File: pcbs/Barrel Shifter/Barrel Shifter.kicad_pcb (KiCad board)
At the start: 2 copper layers, 33 parts, among them U1001 74HC245, U1002 74HC245, U201 74HC138, U301 74HC245, U302 74HC245, U401 74HC245, U402 74HC245, U501 74HC245, U502 74HC245, U601 74HC245, U602 74HC245, U701 74HC245, U702 74HC245, U801 74HC245, U802 74HC245, U901 74HC245, U902 74HC245

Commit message: Second row
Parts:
- added D1201: Blue, LED_SMD:LED_0603_1608Metric, F.Cu at (73.3, 91.5)
- added D1301: Blue, LED_SMD:LED_0603_1608Metric, F.Cu at (101.2, 91.5)
- added D1401: Blue, LED_SMD:LED_0603_1608Metric, F.Cu at (126.0, 91.5)
- added D1501: Blue, LED_SMD:LED_0603_1608Metric, F.Cu at (149.5, 92.1)
- added D1601: Blue, LED_SMD:LED_0603_1608Metric, F.Cu at (175.5, 90.2)
- added D1701: Blue, LED_SMD:LED_0603_1608Metric, F.Cu at (201.5, 91.5)
- added D1801: Blue, LED_SMD:LED_0603_1608Metric, F.Cu at (225.7, 90.2)
- added D1901: Blue, LED_SMD:LED_0603_1608Metric, F.Cu at (252.3, 90.8)
- added R1201: 4k7, Resistor_SMD:R_0603_1608Metric, F.Cu at (77.3, 91.4)
- added R1301: 4k7, Resistor_SMD:R_0603_1608Metric, F.Cu at (105.2, 91.4)
- added R1401: 4k7, Resistor_SMD:R_0603_1608Metric, F.Cu at (130.0, 91.4)
- added R1501: 4k7, Resistor_SMD:R_0603_1608Metric, F.Cu at (153.5, 92.1)
- added R1601: 4k7, Resistor_SMD:R_0603_1608Metric, F.Cu at (179.5, 90.2)
- added R1701: 4k7, Resistor_SMD:R_0603_1608Metric, F.Cu at (205.6, 91.4)
- added R1801: 4k7, Resistor_SMD:R_0603_1608Metric, F.Cu at (229.7, 90.2)
- added R1901: 4k7, Resistor_SMD:R_0603_1608Metric, F.Cu at (256.4, 90.8)
- added U1201: 74HC245, Package_SO:SOIC-20W_7.5x12.8mm_P1.27mm, F.Cu at (76.2, 101.6)
- added U1202: 74HC245, Package_SO:SOIC-20W_7.5x12.8mm_P1.27mm, F.Cu at (76.2, 115.6)
- added U1301: 74HC245, Package_SO:SOIC-20W_7.5x12.8mm_P1.27mm, F.Cu at (101.6, 101.6)
- added U1302: 74HC245, Package_SO:SOIC-20W_7.5x12.8mm_P1.27mm, F.Cu at (101.6, 115.6)
- added U1401: 74HC245, Package_SO:SOIC-20W_7.5x12.8mm_P1.27mm, F.Cu at (127.0, 101.6)
- added U1402: 74HC245, Package_SO:SOIC-20W_7.5x12.8mm_P1.27mm, F.Cu at (127.0, 115.6)
- added U1501: 74HC245, Package_SO:SOIC-20W_7.5x12.8mm_P1.27mm, F.Cu at (152.4, 101.6)
- added U1502: 74HC245, Package_SO:SOIC-20W_7.5x12.8mm_P1.27mm, F.Cu at (152.4, 115.6)
- added U1601: 74HC245, Package_SO:SOIC-20W_7.5x12.8mm_P1.27mm, F.Cu at (177.8, 101.6)
- added U1602: 74HC245, Package_SO:SOIC-20W_7.5x12.8mm_P1.27mm, F.Cu at (177.8, 115.6)
- added U1701: 74HC245, Package_SO:SOIC-20W_7.5x12.8mm_P1.27mm, F.Cu at (203.2, 101.6)
- added U1702: 74HC245, Package_SO:SOIC-20W_7.5x12.8mm_P1.27mm, F.Cu at (203.2, 115.6)
- added U1801: 74HC245, Package_SO:SOIC-20W_7.5x12.8mm_P1.27mm, F.Cu at (228.6, 101.6)
- added U1802: 74HC245, Package_SO:SOIC-20W_7.5x12.8mm_P1.27mm, F.Cu at (228.6, 115.6)
- added U1901: 74HC245, Package_SO:SOIC-20W_7.5x12.8mm_P1.27mm, F.Cu at (254.0, 101.6)
- added U1902: 74HC245, Package_SO:SOIC-20W_7.5x12.8mm_P1.27mm, F.Cu at (254.0, 115.6)
- added U301: 74HC138, Package_DIP:DIP-16_W7.62mm_Socket, F.Cu at (43.2, 102.2)
- renumbered D901 to D1001, D1001 to D1101, D301 to D401, D401 to D501, D501 to D601, D601 to D701, D701 to D801, D801 to D901, R901 to R1001, R1001 to R1101, R301 to R401, R401 to R501, R501 to R601, R601 to R701, R701 to R801, R801 to R901, U901 to U1001, U902 to U1002, U1001 to U1101, U1002 to U1102, U301 to U401, U302 to U402, U401 to U501, U402 to U502, U501 to U601, U502 to U602, U601 to U701, U602 to U702, U701 to U801, U702 to U802, U801 to U901, U802 to U902
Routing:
- net /Shift Block 0/A0: track 507.6 -> 895.9 mm, vias 16 -> 24
- net /Shift Block 0/A1: track 487.9 -> 857.8 mm, vias 16 -> 24
- net /Shift Block 0/A2: track 470.8 -> 819.7 mm, vias 16 -> 24
- net /Shift Block 0/A3: track 467.0 -> 781.6 mm, vias 16 -> 24
- net /Shift Block 0/A4: track 442.9 -> 743.5 mm, vias 16 -> 24
- net /Shift Block 1/~{Y15}: track 0.00 -> 292.5 mm, vias 0 -> 4
- net /Shift Block 0/A5: track 430.2 -> 705.4 mm, vias 16 -> 24
- net /Shift Block 0/Out15: track 155.6 -> 415.4 mm, vias 0 -> 2
- net /Shift Block 0/Out14: track 155.6 -> 414.2 mm, vias 0 -> 2
- net /Shift Block 0/Out13: track 155.6 -> 412.8 mm, vias 0 -> 2
- net /Shift Block 0/Out12: track 155.6 -> 411.6 mm, vias 0 -> 2
- net /Shift Block 0/Out11: track 155.6 -> 410.3 mm, vias 0 -> 2
- net /Shift Block 0/Out10: track 155.6 -> 409.0 mm, vias 0 -> 2
- net /Shift Block 0/Out9: track 155.6 -> 407.7 mm, vias 0 -> 2
- net /Shift Block 0/Out8: track 155.6 -> 406.5 mm, vias 0 -> 2
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
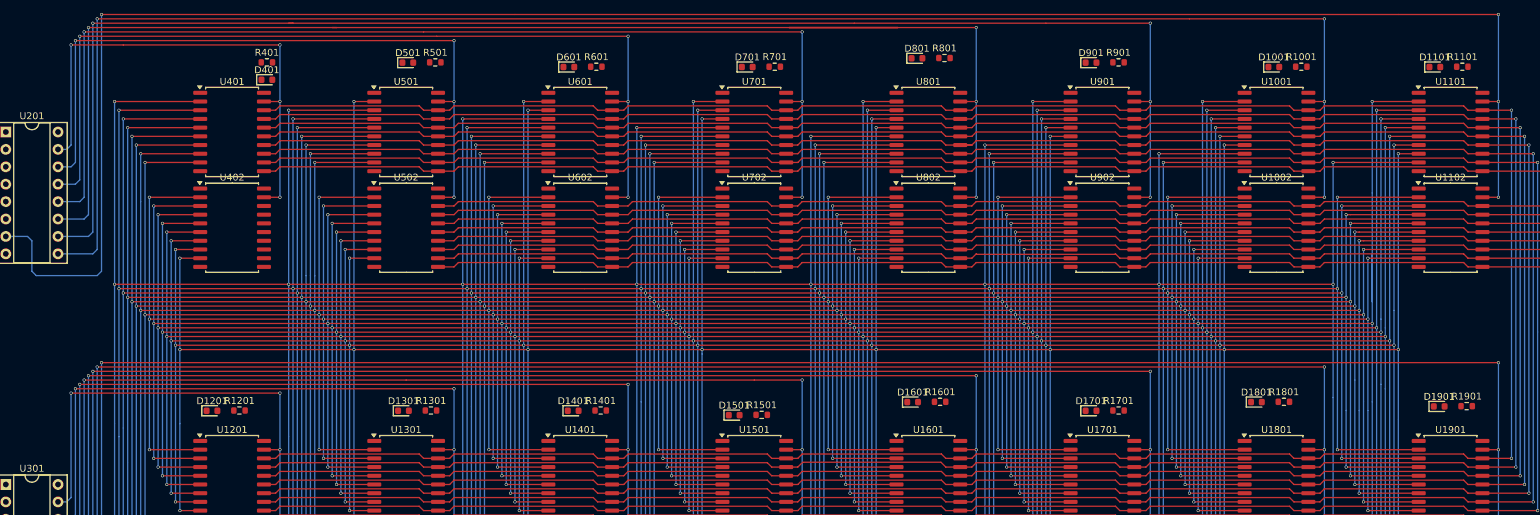
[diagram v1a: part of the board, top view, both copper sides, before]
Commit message: Starting to tidy up the LEDs
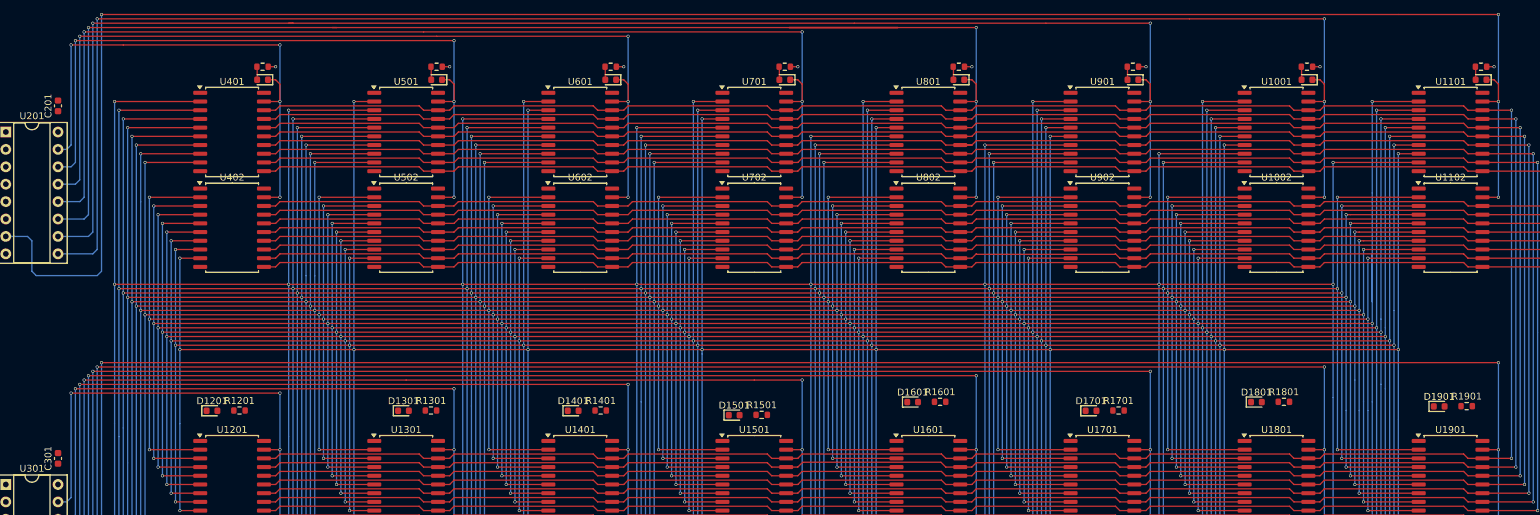
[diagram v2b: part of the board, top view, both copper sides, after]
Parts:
- added C201: C, Capacitor_SMD:C_0603_1608Metric, F.Cu at (50.8, 47.0)
- added C301: C, Capacitor_SMD:C_0603_1608Metric, F.Cu at (50.8, 98.4)
- moved D1101 6.99 mm to (258.4, 43.2), turned to 180 degrees
- moved D801 6.86 mm to (182.2, 43.2), turned to 180 degrees
- moved D901 6.60 mm to (207.6, 43.2), turned to 180 degrees
- moved D601 6.38 mm to (131.4, 43.2), turned to 180 degrees
- moved D701 5.78 mm to (156.8, 43.2), turned to 180 degrees
- moved D1001 5.18 mm to (233.0, 43.2), turned to 180 degrees
- moved D501 4.89 mm to (106.0, 43.2), turned to 180 degrees
- moved R1101 2.73 mm to (258.4, 41.3)
- moved R801 2.45 mm to (182.2, 41.3)
- moved R901 2.19 mm to (207.6, 41.3)
- moved R601 2.09 mm to (131.4, 41.3)
- moved R701 1.46 mm to (156.8, 41.3)
- moved R401 0.90 mm to (80.6, 41.3)
- moved R1001 0.82 mm to (233.0, 41.3)
- moved R501 0.66 mm to (106.0, 41.3)
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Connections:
- U201 pad 5: unconnected-(U201-~{E1}-Pad5) -> /Shift Block 0/~{Enable}
- U301 pad 5: unconnected-(U301-~{E1}-Pad5) -> /Shift Block 1/~{Enable}
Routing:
- net /Shift Block 0/Out8: track 406.5 -> 432.4 mm
- net /Shift Block 0/Out15: track 415.4 -> 441.4 mm
- net /Shift Block 0/Out14: track 414.2 -> 440.1 mm
- net /Shift Block 0/Out9: track 407.7 -> 433.7 mm
- net /Shift Block 0/Out13: track 412.8 -> 438.8 mm
- net /Shift Block 0/Out11: track 410.3 -> 436.2 mm
- net /Shift Block 0/Out10: track 409.0 -> 434.9 mm
- net /Shift Block 0/Out12: track 411.6 -> 437.5 mm
- net +5V: track 0.00 -> 8.64 mm, vias 0 -> 8
- net /Shift Block 0/~{Y5}: track 220.8 -> 225.4 mm
- net /Shift Block 0/~{Y7}: track 291.8 -> 296.4 mm
- net /Shift Block 0/~{Y4}: track 223.4 -> 227.9 mm
- net /Shift Block 0/~{Y2}: track 132.6 -> 137.1 mm
- net /Shift Block 0/~{Y1}: track 103.4 -> 107.9 mm
- net /Shift Block 0/~{Y0}: track 74.1 -> 78.7 mm
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
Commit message: Significant rethinking
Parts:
- removed C201, C301: C, Capacitor_SMD:C_0603_1608Metric
- removed D1001, D1101, D1201, D1301, D1401, D1501, D1601, D1701, D1801, D1901: Blue, LED_SMD:LED_0603_1608Metric
- removed R1001, R1101, R1201, R1301, R1401, R1501, R1601, R1701, R1801, R1901: 4k7, Resistor_SMD:R_0603_1608Metric
- removed U1001, U1002, U1101, U1102, U1201, U1202, U1301, U1302, U1401, U1402, U1501, U1502, U1601, U1602, U1701, U1702, U1801, U1802, U1901, U1902: 74HC245, Package_SO:SOIC-20W_7.5x12.8mm_P1.27mm
- added C101: C, Capacitor_SMD:C_0603_1608Metric, F.Cu at (48.1, 43.2)
- added D201: Blue, LED_SMD:LED_0603_1608Metric, F.Cu at (75.2, 41.3)
- added D301: Blue, LED_SMD:LED_0603_1608Metric, F.Cu at (100.6, 40.7)
- added R201: 4k7, Resistor_SMD:R_0603_1608Metric, F.Cu at (79.2, 41.3)
- added R301: 4k7, Resistor_SMD:R_0603_1608Metric, F.Cu at (104.6, 40.6)
- added U101: 74HC138, Package_DIP:DIP-16_W7.62mm_Socket, F.Cu at (45.7, 50.8)
- added U202: 74HC245, Package_SO:SOIC-20W_7.5x12.8mm_P1.27mm, F.Cu at (76.0, 64.8)
- added U302: 74HC245, Package_SO:SOIC-20W_7.5x12.8mm_P1.27mm, F.Cu at (101.6, 64.8)
- U201, U301: value 74HC138 -> 74HC245; footprint Package_DIP:DIP-16_W7.62mm_Socket -> Package_SO:SOIC-20W_7.5x12.8mm_P1.27mm
- moved U301 77.8 mm to (101.6, 50.8)
- moved D901 75.5 mm to (150.1, 92.1), turned to 0 degrees
- moved D601 74.2 mm to (74.5, 90.8), turned to 0 degrees
- moved D701 74.2 mm to (100.6, 91.5), turned to 0 degrees
- moved R901 73.8 mm to (154.1, 92.1)
- moved D801 73.2 mm to (127.2, 91.5), turned to 0 degrees
- moved R601 72.5 mm to (78.5, 90.8)
- moved R701 72.4 mm to (104.6, 91.4)
- moved U701 71.8 mm to (101.6, 101.6)
- moved U702 71.8 mm to (101.6, 115.6)
- moved U801 71.8 mm to (127.0, 101.6)
- moved U802 71.8 mm to (127.0, 115.6)
- moved U601 71.8 mm to (76.2, 101.6)
- moved U602 71.8 mm to (76.2, 115.6)
- moved U901 71.8 mm to (152.4, 101.6)
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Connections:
- net /Shift Block 0/A0 renamed /A14
- net /Shift Block 0/A10 renamed /A8
- net /Shift Block 0/A11 renamed /A9
- net /Shift Block 0/A12 renamed /A10
- net /Shift Block 0/A13 renamed /A11
- net /Shift Block 0/A14 renamed /A12
- net /Shift Block 0/A15 renamed /A13
- net /Shift Block 0/Out10 renamed /Out10
- net /Shift Block 0/Out11 renamed /Out11
- net /Shift Block 0/Out12 renamed /Out12
- net /Shift Block 0/Out13 renamed /Out13
- net /Shift Block 0/Out14 renamed /Out14
- net /Shift Block 0/Out15 renamed /Out15
- net /Shift Block 0/Out8 renamed /Out8
- net /Shift Block 0/Out9 renamed /Out9
- D401 pad 1: /Shift Block 0/~{Y0} -> /~{Y2}
- D501 pad 1: /Shift Block 0/~{Y1} -> /~{Y3}
- D601 pad 1: /Shift Block 0/~{Y2} -> /~{Y4}
- D701 pad 1: /Shift Block 0/~{Y3} -> /~{Y5}
- D801 pad 1: /Shift Block 0/~{Y4} -> /~{Y6}
- D901 pad 1: /Shift Block 0/~{Y5} -> /~{Y7}
- U201 pad 1: unconnected-(U201-A0-Pad1) -> +5V
- U201 pad 10: /Shift Block 0/~{Y5} -> GND
- U201 pad 11: /Shift Block 0/~{Y4} -> /Out7
- U201 pad 12: /Shift Block 0/~{Y3} -> /Out6
- U201 pad 13: /Shift Block 0/~{Y2} -> /Out5
- U201 pad 14: /Shift Block 0/~{Y1} -> /Out4
- U201 pad 15: /Shift Block 0/~{Y0} -> /Out3
- U201 pad 16: +5V -> /Out2
- U201 pad 2: unconnected-(U201-A1-Pad2) -> /A0
- U201 pad 3: unconnected-(U201-A2-Pad3) -> /A1
- U201 pad 4: unconnected-(U201-~{E0}-Pad4) -> /A2
- U201 pad 5: /Shift Block 0/~{Enable} -> /A3
- U201 pad 6: unconnected-(U201-E2-Pad6) -> /A4
- U201 pad 7: /Shift Block 0/~{Y7} -> /A5
- U201 pad 8: GND -> /A6
- U201 pad 9: /Shift Block 0/~{Y6} -> /A7
- U301 pad 1: unconnected-(U301-A0-Pad1) -> +5V
- U301 pad 10: /Shift Block 1/~{Y13} -> GND
- U301 pad 11: /Shift Block 1/~{Y12} -> /Out7
- U301 pad 12: /Shift Block 1/~{Y11} -> /Out6
- U301 pad 13: /Shift Block 1/~{Y10} -> /Out5
- U301 pad 14: /Shift Block 1/~{Y9} -> /Out4
- U301 pad 15: /Shift Block 1/~{Y8} -> /Out3
- U301 pad 16: +5V -> /Out2
- U301 pad 2: unconnected-(U301-A1-Pad2) -> /A15
- U301 pad 3: unconnected-(U301-A2-Pad3) -> /A0
- U301 pad 4: unconnected-(U301-~{E0}-Pad4) -> /A1
- U301 pad 5: /Shift Block 1/~{Enable} -> /A2
- U301 pad 6: unconnected-(U301-E2-Pad6) -> /A3
- U301 pad 7: /Shift Block 1/~{Y15} -> /A4
- U301 pad 8: GND -> /A5
- U301 pad 9: /Shift Block 1/~{Y14} -> /A6
- U401 pad 11: /Shift Block 0/Out7 -> /Out7
- U401 pad 12: /Shift Block 0/Out6 -> /Out6
- U401 pad 13: /Shift Block 0/Out5 -> /Out5
- U401 pad 14: /Shift Block 0/Out4 -> /Out4
- U401 pad 15: /Shift Block 0/Out3 -> /Out3
- U401 pad 16: /Shift Block 0/Out2 -> /Out2
- U401 pad 17: /Shift Block 0/Out1 -> /Out1
- U401 pad 18: /Shift Block 0/Out0 -> /Out0
- U401 pad 19: /Shift Block 0/~{Y0} -> /~{Y2}
- U401 pad 3: /Shift Block 0/A1 -> /A15
- U401 pad 4: /Shift Block 0/A2 -> /A0
- U401 pad 5: /Shift Block 0/A3 -> /A1
- U401 pad 6: /Shift Block 0/A4 -> /A2
- U401 pad 7: /Shift Block 0/A5 -> /A3
- U401 pad 8: /Shift Block 0/A6 -> /A4
- U401 pad 9: /Shift Block 0/A7 -> /A5
- U402 pad 19: /Shift Block 0/~{Y0} -> /~{Y2}
- U402 pad 2: /Shift Block 0/A8 -> /A6
- U402 pad 3: /Shift Block 0/A9 -> /A7
- U501 pad 11: /Shift Block 0/Out7 -> /Out7
- U501 pad 12: /Shift Block 0/Out6 -> /Out6
- U501 pad 13: /Shift Block 0/Out5 -> /Out5
- U501 pad 14: /Shift Block 0/Out4 -> /Out4
- U501 pad 15: /Shift Block 0/Out3 -> /Out3
- U501 pad 16: /Shift Block 0/Out2 -> /Out2
- U501 pad 17: /Shift Block 0/Out1 -> /Out1
- U501 pad 18: /Shift Block 0/Out0 -> /Out0
- U501 pad 19: /Shift Block 0/~{Y1} -> /~{Y3}
- U501 pad 4: /Shift Block 0/A1 -> /A15
- U501 pad 5: /Shift Block 0/A2 -> /A0
- U501 pad 6: /Shift Block 0/A3 -> /A1
- U501 pad 7: /Shift Block 0/A4 -> /A2
- U501 pad 8: /Shift Block 0/A5 -> /A3
- U501 pad 9: /Shift Block 0/A6 -> /A4
- U502 pad 19: /Shift Block 0/~{Y1} -> /~{Y3}
- U502 pad 2: /Shift Block 0/A7 -> /A5
- U502 pad 3: /Shift Block 0/A8 -> /A6
- U502 pad 4: /Shift Block 0/A9 -> /A7
- U601 pad 11: /Shift Block 0/Out7 -> /Out7
- U601 pad 12: /Shift Block 0/Out6 -> /Out6
- U601 pad 13: /Shift Block 0/Out5 -> /Out5
- U601 pad 14: /Shift Block 0/Out4 -> /Out4
- U601 pad 15: /Shift Block 0/Out3 -> /Out3
- U601 pad 16: /Shift Block 0/Out2 -> /Out2
- U601 pad 17: /Shift Block 0/Out1 -> /Out1
- U601 pad 18: /Shift Block 0/Out0 -> /Out0
- U601 pad 19: /Shift Block 0/~{Y2} -> /~{Y4}
- U601 pad 5: /Shift Block 0/A1 -> /A15
- U601 pad 6: /Shift Block 0/A2 -> /A0
- U601 pad 7: /Shift Block 0/A3 -> /A1
- U601 pad 8: /Shift Block 0/A4 -> /A2
- U601 pad 9: /Shift Block 0/A5 -> /A3
- U602 pad 19: /Shift Block 0/~{Y2} -> /~{Y4}
- U602 pad 2: /Shift Block 0/A6 -> /A4
- U602 pad 3: /Shift Block 0/A7 -> /A5
- U602 pad 4: /Shift Block 0/A8 -> /A6
- U602 pad 5: /Shift Block 0/A9 -> /A7
- U701 pad 11: /Shift Block 0/Out7 -> /Out7
- U701 pad 12: /Shift Block 0/Out6 -> /Out6
- U701 pad 13: /Shift Block 0/Out5 -> /Out5
- U701 pad 14: /Shift Block 0/Out4 -> /Out4
- U701 pad 15: /Shift Block 0/Out3 -> /Out3
- U701 pad 16: /Shift Block 0/Out2 -> /Out2
- U701 pad 17: /Shift Block 0/Out1 -> /Out1
- U701 pad 18: /Shift Block 0/Out0 -> /Out0
- U701 pad 19: /Shift Block 0/~{Y3} -> /~{Y5}
- U701 pad 6: /Shift Block 0/A1 -> /A15
- U701 pad 7: /Shift Block 0/A2 -> /A0
- U701 pad 8: /Shift Block 0/A3 -> /A1
- U701 pad 9: /Shift Block 0/A4 -> /A2
- U702 pad 19: /Shift Block 0/~{Y3} -> /~{Y5}
- U702 pad 2: /Shift Block 0/A5 -> /A3
- U702 pad 3: /Shift Block 0/A6 -> /A4
- U702 pad 4: /Shift Block 0/A7 -> /A5
- U702 pad 5: /Shift Block 0/A8 -> /A6
- U702 pad 6: /Shift Block 0/A9 -> /A7
- U801 pad 11: /Shift Block 0/Out7 -> /Out7
- U801 pad 12: /Shift Block 0/Out6 -> /Out6
- U801 pad 13: /Shift Block 0/Out5 -> /Out5
- U801 pad 14: /Shift Block 0/Out4 -> /Out4
- U801 pad 15: /Shift Block 0/Out3 -> /Out3
- U801 pad 16: /Shift Block 0/Out2 -> /Out2
- U801 pad 17: /Shift Block 0/Out1 -> /Out1
- U801 pad 18: /Shift Block 0/Out0 -> /Out0
- U801 pad 19: /Shift Block 0/~{Y4} -> /~{Y6}
- U801 pad 7: /Shift Block 0/A1 -> /A15
- U801 pad 8: /Shift Block 0/A2 -> /A0
- U801 pad 9: /Shift Block 0/A3 -> /A1
- U802 pad 19: /Shift Block 0/~{Y4} -> /~{Y6}
- U802 pad 2: /Shift Block 0/A4 -> /A2
- U802 pad 3: /Shift Block 0/A5 -> /A3
- U802 pad 4: /Shift Block 0/A6 -> /A4
- U802 pad 5: /Shift Block 0/A7 -> /A5
- U802 pad 6: /Shift Block 0/A8 -> /A6
- U802 pad 7: /Shift Block 0/A9 -> /A7
- U901 pad 11: /Shift Block 0/Out7 -> /Out7
- U901 pad 12: /Shift Block 0/Out6 -> /Out6
- U901 pad 13: /Shift Block 0/Out5 -> /Out5
- U901 pad 14: /Shift Block 0/Out4 -> /Out4
- U901 pad 15: /Shift Block 0/Out3 -> /Out3
- U901 pad 16: /Shift Block 0/Out2 -> /Out2
- U901 pad 17: /Shift Block 0/Out1 -> /Out1
- U901 pad 18: /Shift Block 0/Out0 -> /Out0
- U901 pad 19: /Shift Block 0/~{Y5} -> /~{Y7}
- U901 pad 8: /Shift Block 0/A1 -> /A15
- U901 pad 9: /Shift Block 0/A2 -> /A0
- U902 pad 19: /Shift Block 0/~{Y5} -> /~{Y7}
- U902 pad 2: /Shift Block 0/A3 -> /A1
- U902 pad 3: /Shift Block 0/A4 -> /A2
- U902 pad 4: /Shift Block 0/A5 -> /A3
- U902 pad 5: /Shift Block 0/A6 -> /A4
- U902 pad 6: /Shift Block 0/A7 -> /A5
- U902 pad 7: /Shift Block 0/A8 -> /A6
- U902 pad 8: /Shift Block 0/A9 -> /A7
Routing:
- net /Shift Block 0/A1: track 857.8 -> 0.00 mm, vias 24 -> 0
- net /Shift Block 0/A2: track 819.7 -> 0.00 mm, vias 24 -> 0
- net /Shift Block 0/A3: track 781.6 -> 0.00 mm, vias 24 -> 0
- net /Shift Block 0/A4: track 743.5 -> 0.00 mm, vias 24 -> 0
- net /Shift Block 0/A5: track 705.4 -> 0.00 mm, vias 24 -> 0
- net /Shift Block 0/A6: track 667.3 -> 0.00 mm, vias 24 -> 0
- net /Shift Block 0/A7: track 629.2 -> 0.00 mm, vias 24 -> 0
- net /Shift Block 0/A9: track 622.8 -> 0.00 mm, vias 24 -> 0
- net /A14: track 895.9 -> 273.1 mm, vias 24 -> 12
- net /Shift Block 0/A8: track 591.1 -> 0.00 mm, vias 24 -> 0
- net /A12: track 697.8 -> 232.4 mm, vias 24 -> 12
- net /A13: track 715.5 -> 252.8 mm, vias 24 -> 12
- net /Shift Block 0/Out7: track 431.1 -> 0.00 mm, vias 2 -> 0
- net /Shift Block 0/Out6: track 429.9 -> 0.00 mm, vias 2 -> 0
- net /Shift Block 0/Out4: track 429.4 -> 0.00 mm, vias 2 -> 0
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
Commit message: Almost there...
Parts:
- added J101: ~, BoardEdgeConnectors:TE-5530843-4-Edge, F.Cu at (25.4, 78.7)
- moved D401 6.99 mm to (131.4, 42.5), turned to 180 degrees
- moved D501 6.86 mm to (156.8, 42.5), turned to 180 degrees
- moved D901 6.85 mm to (156.8, 93.3), turned to 180 degrees
- moved D601 6.60 mm to (80.6, 93.3), turned to 180 degrees
- moved C101 6.11 mm to (53.3, 46.4), turned to 90 degrees
- moved D301 5.78 mm to (106.0, 42.5), turned to 180 degrees
- moved D701 5.78 mm to (106.0, 93.3), turned to 180 degrees
- moved D201 5.61 mm to (80.6, 42.5), turned to 180 degrees
- moved D801 4.60 mm to (131.4, 93.3), turned to 180 degrees
- moved R901 2.80 mm to (156.8, 91.4)
- moved R401 2.73 mm to (131.4, 40.6)
- moved R501 2.45 mm to (156.8, 40.6)
- moved R601 2.19 mm to (80.6, 91.4)
- moved R201 1.59 mm to (80.6, 40.6)
- moved R301 1.46 mm to (106.0, 40.6)
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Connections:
- net /Out0 renamed /C0
- net /Out1 renamed /C1
- net /Out10 renamed /C10
- net /Out11 renamed /C11
- net /Out12 renamed /C12
- net /Out13 renamed /C13
- net /Out14 renamed /C14
- net /Out15 renamed /C15
- net /Out2 renamed /C2
- net /Out3 renamed /C3
- net /Out4 renamed /C4
- net /Out5 renamed /C5
- net /Out6 renamed /C6
- net /Out7 renamed /C7
- net /Out8 renamed /C8
- net /Out9 renamed /C9
- U101 pad 1: unconnected-(U101-A0-Pad1) -> /B_0
- U101 pad 2: unconnected-(U101-A1-Pad2) -> /B_1
- U101 pad 3: unconnected-(U101-A2-Pad3) -> /B_2
- U101 pad 4: unconnected-(U101-~{E0}-Pad4) -> /B_3
- U101 pad 5: /~{Enable} -> /~{OE}
- U101 pad 6: unconnected-(U101-E2-Pad6) -> +5V
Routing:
- net /C12: track 77.8 -> 379.0 mm, vias 0 -> 3
- net /C8: track 77.8 -> 373.3 mm, vias 0 -> 3
- net /C10: track 77.8 -> 372.0 mm, vias 0 -> 3
- net /C14: track 77.8 -> 370.1 mm, vias 0 -> 3
- net /C3: track 77.8 -> 366.6 mm, vias 0 -> 3
- net /C2: track 77.8 -> 360.6 mm, vias 0 -> 3
- net /C4: track 77.8 -> 359.9 mm, vias 0 -> 3
- net /C6: track 77.8 -> 358.6 mm, vias 0 -> 3
- net /C9: track 77.8 -> 356.5 mm, vias 0 -> 3
- net /C13: track 77.8 -> 356.5 mm, vias 0 -> 3
- net /C11: track 77.8 -> 355.8 mm, vias 0 -> 3
- net /C0: track 103.7 -> 369.4 mm, vias 0 -> 3
- net /C5: track 77.8 -> 340.6 mm, vias 0 -> 3
- net /C1: track 77.8 -> 340.0 mm, vias 0 -> 3
- net +5V: track 0.00 -> 225.9 mm, vias 0 -> 25
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- added copper zone on B.Cu, net +5V
- added copper zone on F.Cu, net GND
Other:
- board outline added: 132.1 x 100.3 mm
- board text added: "Barrel Shifter"
- board text added: "JLCJLCJLCJLC"
- board text added: "RGE2024"

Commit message: Finishing connection
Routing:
- net GND: track 6.25 -> 41.2 mm, vias 0 -> 16
- net /C1: track 340.0 -> 369.6 mm, vias 3 -> 4
- net /C3: track 366.6 -> 395.0 mm, vias 3 -> 4
- net /C5: track 340.6 -> 367.7 mm, vias 3 -> 4
- net /C7: track 340.6 -> 366.4 mm, vias 3 -> 4
- net /C9: track 356.5 -> 381.0 mm, vias 3 -> 4
- net /C11: track 355.8 -> 379.8 mm, vias 3 -> 4
- net /C13: track 356.5 -> 379.1 mm, vias 3 -> 4
- net /C15: track 357.7 -> 377.9 mm, vias 3 -> 4
- net /A1: track 432.3 -> 450.5 mm, vias 12 -> 13
- net /A3: track 431.1 -> 448.0 mm, vias 12 -> 13
- net /A5: track 422.2 -> 437.8 mm, vias 12 -> 13
- net /A7: track 405.7 -> 420.1 mm, vias 12 -> 13
- net /A9: track 369.5 -> 382.0 mm, vias 12 -> 13
- net /A11: track 311.7 -> 323.5 mm, vias 12 -> 13
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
